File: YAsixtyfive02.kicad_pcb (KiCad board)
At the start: 2 copper layers, 99.7 x 99.7 mm, 49 parts, among them J1 ~{NMI}, J2 Aux 5VDC, J3 Power 5V, J4 Expansion Bus, J5 Port A, J6 Port B, J7 GND, J8 FTDI Serial2USB, SW1 RESET, U1 WD65C02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

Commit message: PCB take 1 v1.5.2 Complete VIA + ACIA
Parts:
- moved R10 12.9 mm to (50.1, 86.3), turned to 180 degrees
- moved R9 7.57 mm to (50.0, 82.8), turned to 180 degrees
- moved TP1 5.32 mm to (106.3, 54.6)
- moved JP1 5.08 mm to (106.2, 62.0)
- moved J1 2.19 mm to (106.0, 75.3)
- moved R11 1.47 mm to (70.8, 85.1)
- moved R12 1.31 mm to (60.6, 88.2)
- moved R8 0.29 mm to (121.3, 141.3)
- moved R6 0.28 mm to (127.5, 131.1)
- moved R7 0.26 mm to (124.4, 131.1)
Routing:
- net a4: track 0.00 -> 197.0 mm, vias 0 -> 4
- net a3: track 0.00 -> 194.5 mm, vias 0 -> 4
- net a13: track 0.00 -> 172.2 mm, vias 0 -> 6
- net ~{RESET}: track 0.00 -> 171.9 mm, vias 0 -> 3
- net EXP_IRQ: track 0.00 -> 171.0 mm, vias 0 -> 1
- net d7: track 0.00 -> 170.1 mm, vias 0 -> 5
- net a0: track 0.00 -> 167.9 mm, vias 0 -> 3
- net a1: track 0.00 -> 166.7 mm, vias 0 -> 3
- net d5: track 0.00 -> 166.6 mm, vias 0 -> 6
- net d3: track 0.00 -> 164.5 mm, vias 0 -> 6
- net d4: track 0.00 -> 164.5 mm, vias 0 -> 6
- net R~{W}: track 0.00 -> 163.6 mm, vias 0 -> 6
- net a2: track 0.00 -> 163.3 mm, vias 0 -> 3
- net d6: track 0.00 -> 161.2 mm, vias 0 -> 4
- net ~{VIA2_IRQ}: track 0.00 -> 155.7 mm, vias 0 -> 1
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
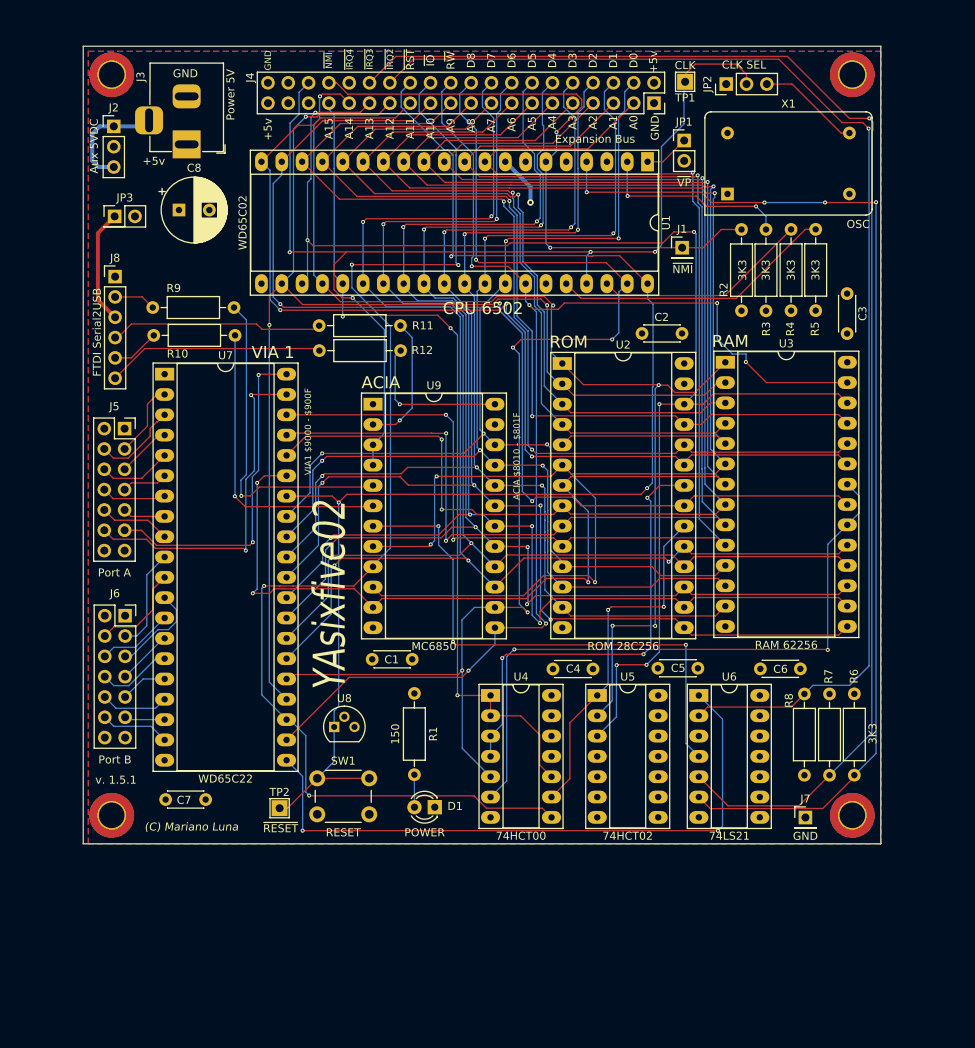
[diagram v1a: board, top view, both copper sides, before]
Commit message: Board cleanup, renders and add backups to gitignore
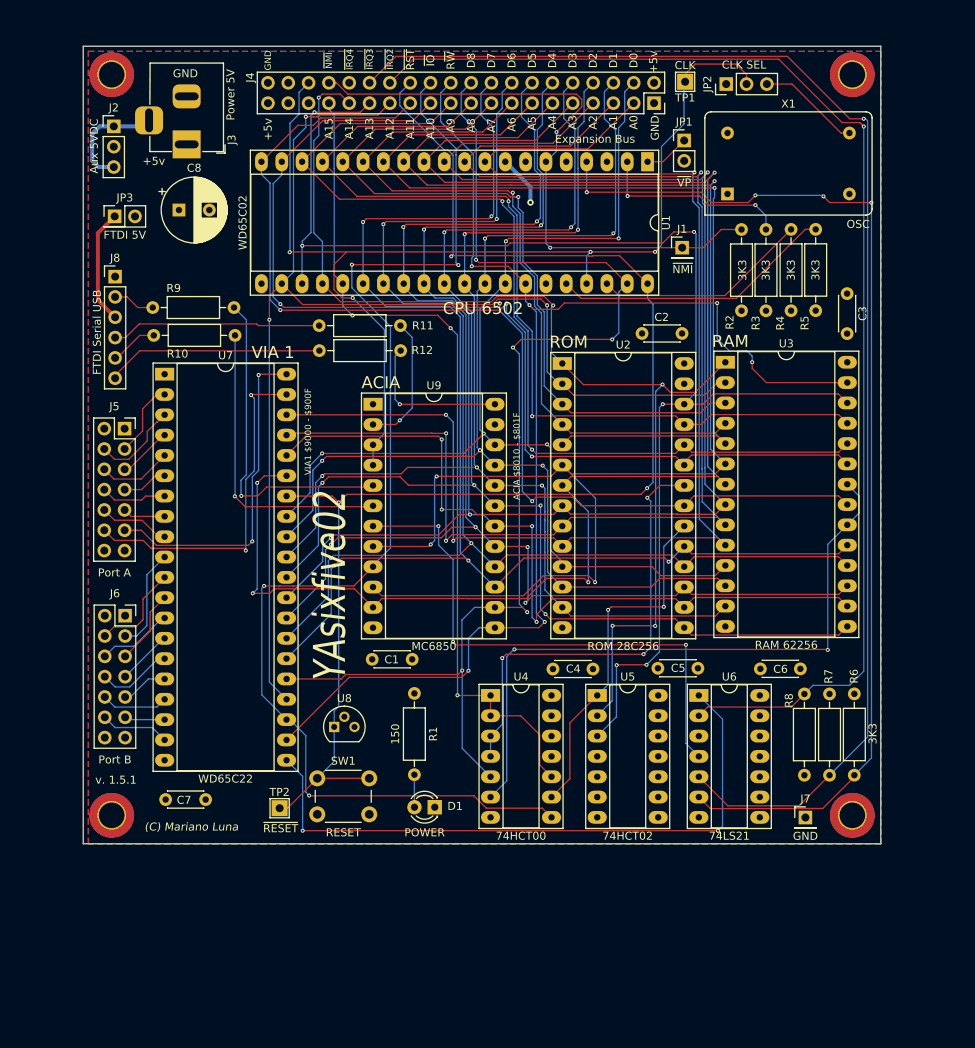
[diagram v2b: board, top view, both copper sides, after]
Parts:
- J8: value FTDI Serial2USB -> FTDI Serial USB
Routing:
- net a3: track 194.5 -> 197.3 mm
- net PB2: track 11.8 -> 9.38 mm
- net a2: track 163.3 -> 165.2 mm
- net R~{W}: track 163.6 -> 164.8 mm
- net a1: track 166.7 -> 167.9 mm
- net a4: track 197.0 -> 198.0 mm
- net a15: track 107.5 -> 106.6 mm
- net EXP_IRQ: track 171.0 -> 170.2 mm
- net ~{VIA2_IRQ}: track 155.7 -> 155.0 mm
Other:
- board text added: "+ JP1: Closed NMOS | Open CMOS + JP2: 1. GND | 2. PHI2 IN | 3. OSC OUT 1Mhz + JP3: Power via USB + J1: ~{NMI} IN"
- board text added: "- RAM $0000-$7FFF 32K - I/O $8000-$9FFF 8K + ACIA $8010-$801F + VIA1 $9000-$900F - ROM $A000-$FFFF 24K"
- board text removed: "+ JP1: Closed NMOS | Open CMOS + JP2: 1. GND | 2. PHI2 IN | 3. OSC OUT 1Mhz + J1: ~{NMI} IN"
- board text removed: "- RAM $0000-$7FFF 32K - I/O $8000-$9FFF 8K + VIA1 $9000-$900F - ROM $A000-$FFFF 24K"

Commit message: changed PHI2 out to CLK and PCB tweaks
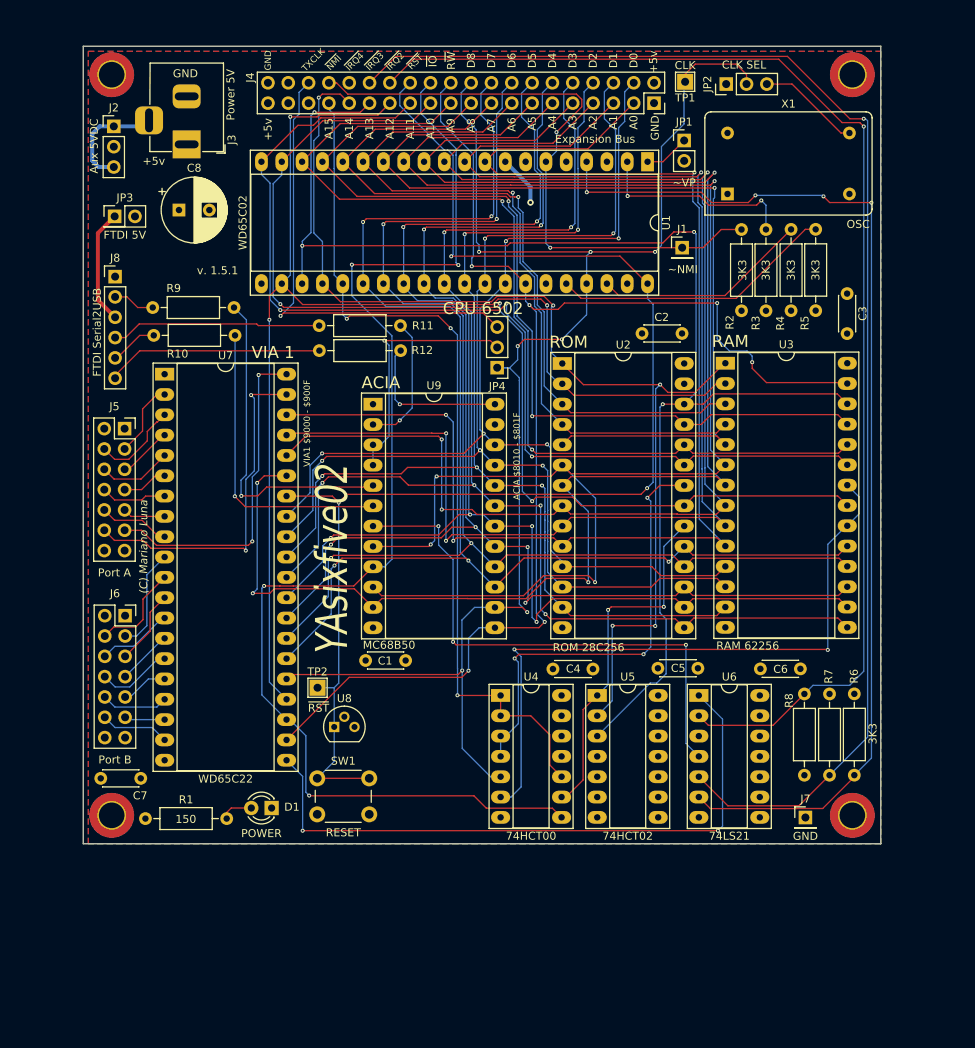
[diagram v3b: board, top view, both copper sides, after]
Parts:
- added JP4: ACIA CLK SEL, Connector_PinHeader_2.54mm:PinHeader_1x03_P2.54mm_Vertical, F.Cu at (82.9, 90.3)
- J1: value ~{NMI} -> ~NMI
- J8: value FTDI Serial USB -> FTDI Serial2USB
- JP1: value ~{VP} -> ~VP
- TP2: value ~{RESET} -> ~{RST}
- U9: value MC6850 -> MC68B50
- moved R1 37.1 mm to (38.9, 146.7), turned to 0 degrees
- moved D1 20.4 mm to (54.7, 145.4)
- moved TP2 15.8 mm to (60.4, 130.4)
- moved C7 4.09 mm to (38.3, 141.7), turned to 180 degrees
- moved U4 1.26 mm to (83.3, 131.3)
- moved C1 0.84 mm to (66.4, 126.9)
- moved U3 0.12 mm to (111.4, 89.8)
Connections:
- J4 pad 20: PHI2 -> CLK
- J4 pad 32: Net-(J4-Pad32) -> unconnected-(J4-Pad32)
- J4 pad 35: Net-(J4-Pad35) -> unconnected-(J4-Pad35)
- J4 pad 36: CLK -> ACIA_CLK
- J4 pad 37: Net-(J4-Pad37) -> unconnected-(J4-Pad37)
- J4 pad 38: Net-(J4-Pad38) -> unconnected-(J4-Pad38)
- U1 pad 3: Net-(U1-Pad3) -> unconnected-(U1-Pad3)
- U1 pad 35: Net-(U1-Pad35) -> unconnected-(U1-Pad35)
- U1 pad 39: PHI2 -> unconnected-(U1-Pad39)
- U1 pad 5: Net-(U1-Pad5) -> unconnected-(U1-Pad5)
- U1 pad 7: Net-(U1-Pad7) -> unconnected-(U1-Pad7)
- U4 pad 11: Net-(U4-Pad11) -> unconnected-(U4-Pad11)
- U4 pad 5: PHI2 -> CLK
- U5 pad 10: Net-(U5-Pad10) -> unconnected-(U5-Pad10)
- U5 pad 13: Net-(U5-Pad13) -> unconnected-(U5-Pad13)
- U5 pad 4: Net-(U5-Pad4) -> unconnected-(U5-Pad4)
- U6 pad 8: Net-(U6-Pad8) -> unconnected-(U6-Pad8)
- U7 pad 25: PHI2 -> CLK
- U9 pad 14: PHI2 -> CLK
- U9 pad 3: CLK -> /TX_CLK
- U9 pad 4: CLK -> /TX_CLK
- X1 pad 1: Net-(X1-Pad1) -> unconnected-(X1-Pad1)
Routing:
- net PHI2: track 150.5 -> 0.00 mm, vias 5 -> 0
- net ACIA_CLK: track 0.00 -> 58.5 mm, vias 0 -> 1
- net CLK: track 137.0 -> 188.0 mm, vias 4 -> 7
- net /TX_CLK: track 0.00 -> 31.6 mm, vias 0 -> 1
- net ~{RESET}: track 172.1 -> 167.8 mm
- net ~{IO_CS}: track 154.3 -> 156.5 mm
- net a15: track 106.6 -> 108.8 mm
- net Net-(R3-Pad2): track 24.3 -> 25.6 mm
- net a12: track 154.1 -> 155.2 mm
- net a13: track 172.4 -> 171.5 mm, vias 6 -> 4
- net ~{VIA2_IRQ}: track 155.0 -> 155.9 mm
- net ~{RAM_CS}: track 81.9 -> 82.8 mm
- net ~{ROM_OE}: track 56.1 -> 55.4 mm
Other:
- board text added: "+ JP1: Closed NMOS | Open CMOS + JP2: 1. GND | 2. PHI2 IN | 3. OSC OUT + JP3: Power via USB + J1: ~{NMI} IN"
- board text added: "TXCLK"
- board text removed: "+ JP1: Closed NMOS | Open CMOS + JP2: 1. GND | 2. PHI2 IN | 3. OSC OUT 1Mhz + JP3: Power via USB + J1: ~{NMI} IN"

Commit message: COmponents placed ready to route
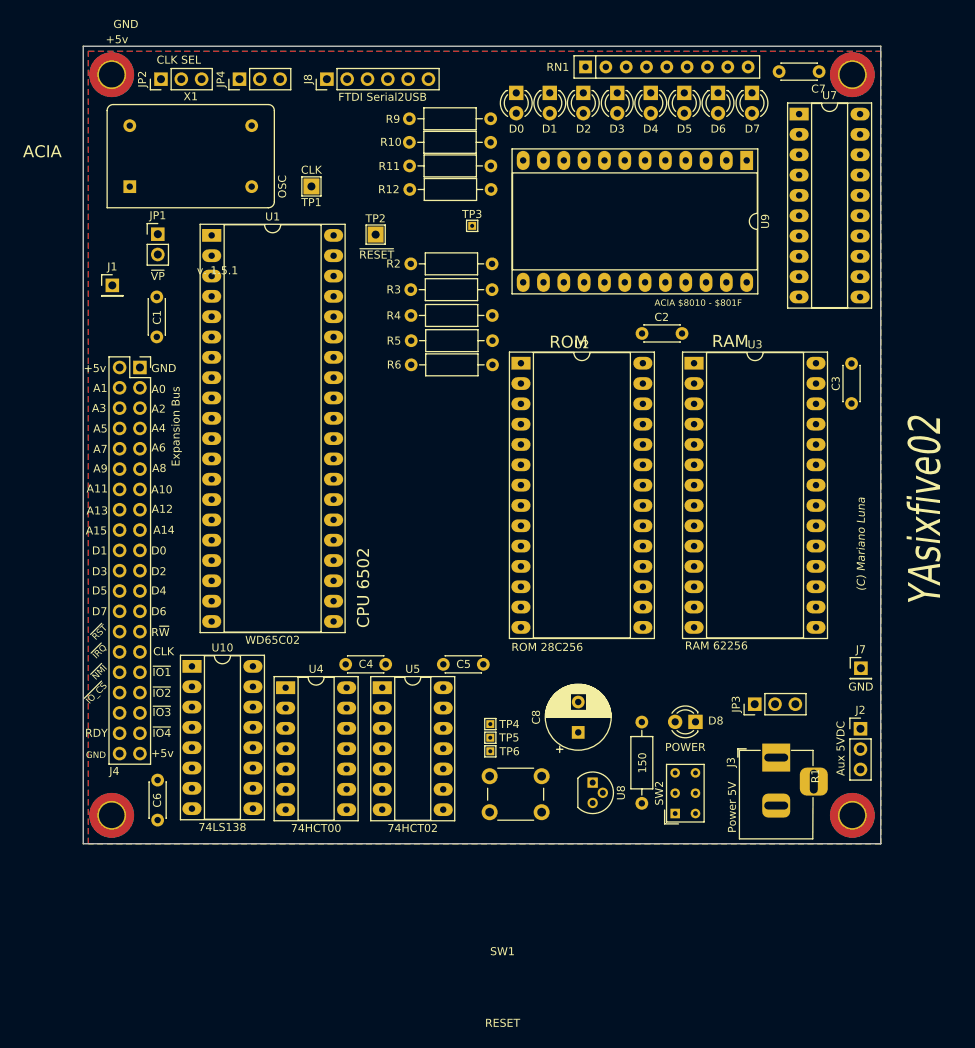
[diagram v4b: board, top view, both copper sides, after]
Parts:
- removed J5: Port A, Connector_PinSocket_2.54mm:PinSocket_2x07_P2.54mm_Vertical
- removed J6: Port B, Connector_PinSocket_2.54mm:PinSocket_2x07_P2.54mm_Vertical
- removed R7, R8: 3K3, Resistor_THT:R_Axial_DIN0207_L6.3mm_D2.5mm_P10.16mm_Horizontal
- removed U6: 74LS21, Package_DIP:DIP-14_W7.62mm_Socket_LongPads
- added D0: CTL_0, LED_THT:LED_D3.0mm, F.Cu at (85.2, 56.0)
- added D1: CTL_1, LED_THT:LED_D3.0mm, F.Cu at (89.4, 56.0)
- added D2: CTL_2, LED_THT:LED_D3.0mm, F.Cu at (93.6, 56.0)
- added D3: 3, LED_THT:LED_D3.0mm, F.Cu at (97.9, 56.0)
- added D4: 3, LED_THT:LED_D3.0mm, F.Cu at (102.1, 56.0)
- added D5: 3, LED_THT:LED_D3.0mm, F.Cu at (106.2, 56.0)
- added D6: 3, LED_THT:LED_D3.0mm, F.Cu at (110.5, 56.0)
- added D7: 3, LED_THT:LED_D3.0mm, F.Cu at (114.7, 56.0)
- added RN1: R_Network08, Resistor_THT:R_Array_SIP9, F.Cu at (93.9, 52.8)
- added SW2: SW_Push_DPDT, Button_Switch_THT:SW_NKK_GW12LJP, F.Cu at (105.1, 146.1)
- added TP3: IO7, TestPoint:TestPoint_THTPad_1.0x1.0mm_Drill0.5mm, F.Cu at (79.7, 72.6)
- added TP4: IO5, TestPoint:TestPoint_THTPad_1.0x1.0mm_Drill0.5mm, F.Cu at (82.0, 134.9)
- added TP5: IO6, TestPoint:TestPoint_THTPad_1.0x1.0mm_Drill0.5mm, F.Cu at (82.0, 136.6)
- added TP6: IO7, TestPoint:TestPoint_THTPad_1.0x1.0mm_Drill0.5mm, F.Cu at (82.0, 138.3)
- added U10: 74LS138, Package_DIP:DIP-16_W7.62mm_Socket_LongPads, F.Cu at (44.7, 127.7)
- J1: value ~NMI -> ~{NMI}
- JP1: value ~VP -> ~{VP}
- JP3: value FTDI 5V -> Aux 5VDC; footprint Connector_PinHeader_2.54mm:PinHeader_2x01_P2.54mm_Vertical -> Connector_PinHeader_2.54mm:PinHeader_1x03_P2.54mm_Vertical
- TP2: value ~{RST} -> ~{RESET}
- U7: value WD65C22 -> 74HCT273; footprint Package_DIP:DIP-40_W15.24mm_Socket_LongPads -> Package_DIP:DIP-20_W7.62mm_Socket_LongPads
- U9: value MC68B50 -> MC6850_
- moved C7 122.5 mm to (123.1, 53.3)
- moved J2 119.9 mm to (128.3, 135.5)
- moved J3 106.3 mm to (117.7, 139.1), turned to 90 degrees
- moved JP3 100.6 mm to (115.1, 132.4), turned to 90 degrees
- moved U7 85.7 mm to (120.6, 58.6)
- moved C8 82.2 mm to (93.0, 135.9), turned to 90 degrees
- moved C6 76.6 mm to (40.4, 141.9), turned to -90 degrees
- moved X1 74.7 mm to (36.9, 67.7)
- moved J4 72.3 mm to (38.2, 90.3), turned to 0 degrees
- moved J1 71.4 mm to (34.7, 80.1)
- moved JP2 70.7 mm to (40.8, 54.3)
- moved R6 69.0 mm to (72.1, 90.0), turned to 0 degrees
- moved JP1 66.8 mm to (40.4, 73.7)
- moved R1 62.1 mm to (100.9, 144.8), turned to 90 degrees
- moved TP2 57.1 mm to (67.7, 73.7)
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- renumbered D1 to D8
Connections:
- net Net-(J8-Pad3) renamed USB_5V
- J3 pad 1: +5V -> EXT_5V
- J4 pad 10: d3 -> a7
- J4 pad 11: a4 -> a8
- J4 pad 12: d4 -> a9
- J4 pad 13: a5 -> a10
- J4 pad 14: d5 -> a11
- J4 pad 15: a6 -> a12
- J4 pad 16: d6 -> a13
- J4 pad 17: a7 -> a14
- J4 pad 18: d7 -> a15
- J4 pad 19: a8 -> d0
- J4 pad 20: CLK -> d1
- J4 pad 21: a9 -> d2
- J4 pad 22: R~{W} -> d3
- J4 pad 23: a10 -> d4
- J4 pad 24: ~{IO_CS} -> d5
- J4 pad 25: a11 -> d6
- J4 pad 26: ~{RESET} -> d7
- J4 pad 27: a12 -> R~{W}
- J4 pad 28: ~{VIA2_IRQ} -> ~{RESET}
- J4 pad 29: a13 -> CLK
- J4 pad 30: EXP_IRQ -> ~{IRQ}
- J4 pad 31: a14 -> ~{IO_1}
- J4 pad 32: unconnected-(J4-Pad32) -> ~{NMI}
- J4 pad 33: a15 -> ~{IO_2}
- J4 pad 34: ~{NMI} -> ~{IO_CS}
- J4 pad 35: unconnected-(J4-Pad35) -> ~{IO_3}
- J4 pad 36: ACIA_CLK -> unconnected-(J4-Pad36)
- J4 pad 37: unconnected-(J4-Pad37) -> ~{IO_4}
- J4 pad 38: unconnected-(J4-Pad38) -> RDY
- J4 pad 4: d0 -> a1
- J4 pad 5: a1 -> a2
- J4 pad 6: d1 -> a3
- J4 pad 7: a2 -> a4
- J4 pad 8: d2 -> a5
- J4 pad 9: a3 -> a6
- R2 pad 2: ~{NMI} -> ~{IRQ}
- R3 pad 2: Net-(R3-Pad2) -> ~{NMI}
- R4 pad 1: +5V -> BE
- R4 pad 2: Net-(R4-Pad2) -> +5V
- R5 pad 2: Net-(R5-Pad2) -> RDY
- R6 pad 1: +5V -> ~{SO}
- R6 pad 2: ~{IRQ} -> +5V
- U1 pad 2: Net-(R3-Pad2) -> RDY
- U1 pad 36: Net-(R5-Pad2) -> BE
- U1 pad 38: Net-(R4-Pad2) -> ~{SO}
- U7 pad 1: GND -> ~{RESET}
- U7 pad 10: PB0 -> GND
- U7 pad 11: PB1 -> ~{IO_8}
- U7 pad 12: PB2 -> Net-(D4-Pad2)
- U7 pad 13: PB3 -> d4
- U7 pad 14: PB4 -> d5
- U7 pad 15: PB5 -> Net-(D5-Pad2)
- U7 pad 16: PB6 -> Net-(D6-Pad2)
- U7 pad 17: PB7 -> d6
- U7 pad 18: CB1 -> d7
- U7 pad 19: CB2 -> Net-(D7-Pad2)
- U7 pad 2: PA0 -> Net-(D0-Pad2)
- U7 pad 3: PA1 -> d0
- U7 pad 4: PA2 -> d1
- U7 pad 5: PA3 -> Net-(D1-Pad2)
- U7 pad 6: PA4 -> Net-(D2-Pad2)
- U7 pad 7: PA5 -> d2
- U7 pad 8: PA6 -> d3
- U7 pad 9: PA7 -> Net-(D3-Pad2)
- U9 pad 11: a3 -> a0
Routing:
- net a4: track 198.0 -> 0.00 mm, vias 4 -> 0
- net a3: track 197.5 -> 0.00 mm, vias 4 -> 0
- net CLK: track 188.0 -> 0.00 mm, vias 7 -> 0
- net a13: track 171.5 -> 0.00 mm, vias 4 -> 0
- net d7: track 170.3 -> 0.00 mm, vias 5 -> 0
- net EXP_IRQ: track 170.2 -> 0.00 mm, vias 1 -> 0
- net a0: track 168.5 -> 0.00 mm, vias 3 -> 0
- net a1: track 168.0 -> 0.00 mm, vias 3 -> 0
- net ~{RESET}: track 167.8 -> 0.00 mm, vias 3 -> 0
- net d5: track 166.9 -> 0.00 mm, vias 6 -> 0
- net a2: track 165.3 -> 0.00 mm, vias 3 -> 0
- net R~{W}: track 164.8 -> 0.00 mm, vias 6 -> 0
- net d3: track 164.6 -> 0.00 mm, vias 6 -> 0
- net d4: track 164.0 -> 0.00 mm, vias 6 -> 0
- net d6: track 161.1 -> 0.00 mm, vias 4 -> 0
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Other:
- board text added: "CLK"
- board text added: "RDY"
- board text added: "~{IO1}"
- board text added: "~{IO2}"
- board text added: "~{IO3}"
- board text added: "~{IO4}"
- board text added: "~{IO_CS}"
- board text added: "~{IRQ}"
- board text removed: "D8"
- board text removed: "TXCLK"
- board text removed: "VIA 1"
- board text removed: "VIA1 $9000 - $900F"
- board text removed: "~{IO}"
- board text removed: "~{IRQ2}"
- board text removed: "~{IRQ3}"
- board text removed: "~{IRQ4}"
